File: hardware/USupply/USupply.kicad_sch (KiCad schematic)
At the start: 11 parts, among them P1 USB_C_Receptacle_USB2.0, Q1 Si2319CDS, U1 HUSB238

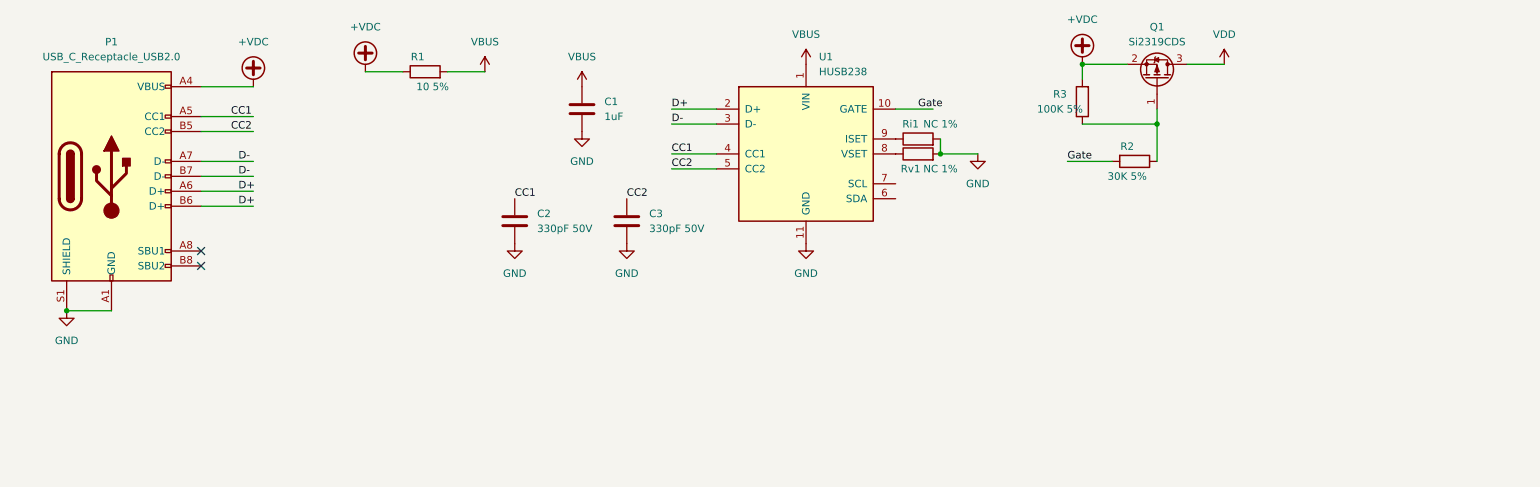
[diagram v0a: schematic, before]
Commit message: refactor(hw/usb): refine usb pd by sub
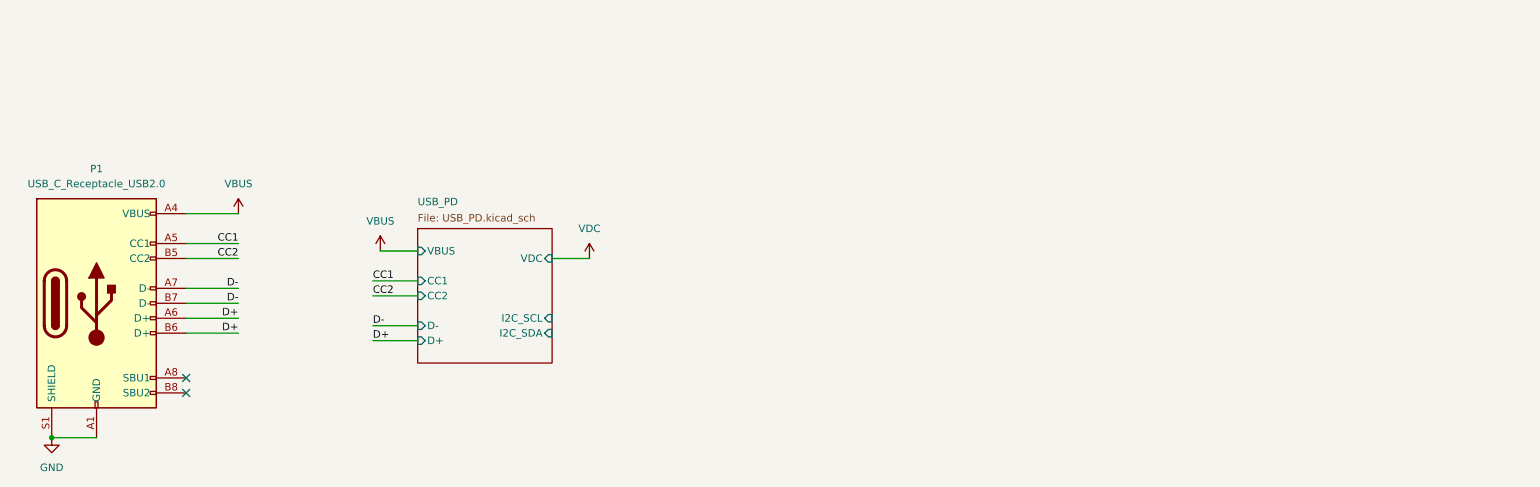
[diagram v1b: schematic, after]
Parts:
- removed C1: 1uF, Capacitor_SMD:C_0603_1608Metric_Pad1.08x0.95mm_HandSolder, symbol Device:C
- removed C2, C3: 330pF 50V, Capacitor_SMD:C_0603_1608Metric_Pad1.08x0.95mm_HandSolder, symbol Device:C
- removed Q1: Si2319CDS, Package_TO_SOT_SMD:SOT-23, symbol Transistor_FET:Si2319CDS
- removed R1: 10 5%, Resistor_SMD:R_0603_1608Metric, symbol Device:R
- removed R2: 30K 5%, Resistor_SMD:R_0603_1608Metric, symbol Device:R
- removed R3: 100K 5%, Resistor_SMD:R_0603_1608Metric, symbol Device:R
- removed Ri1, Rv1: NC 1%, Resistor_SMD:R_0603_1608Metric, symbol Device:R
- removed U1: HUSB238, Package_DFN_QFN:DFN-10-1EP_3x3mm_P0.5mm_EP1.7x2.5mm, symbol Power_Management:STM6600
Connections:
- net +VDC is gone; now on net VBUS: P1.A4 (VBUS), P1.A9 (VBUS), P1.B4 (VBUS), P1.B9 (VBUS)
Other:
- added sheet USB_PD (USB_PD.kicad_sch)

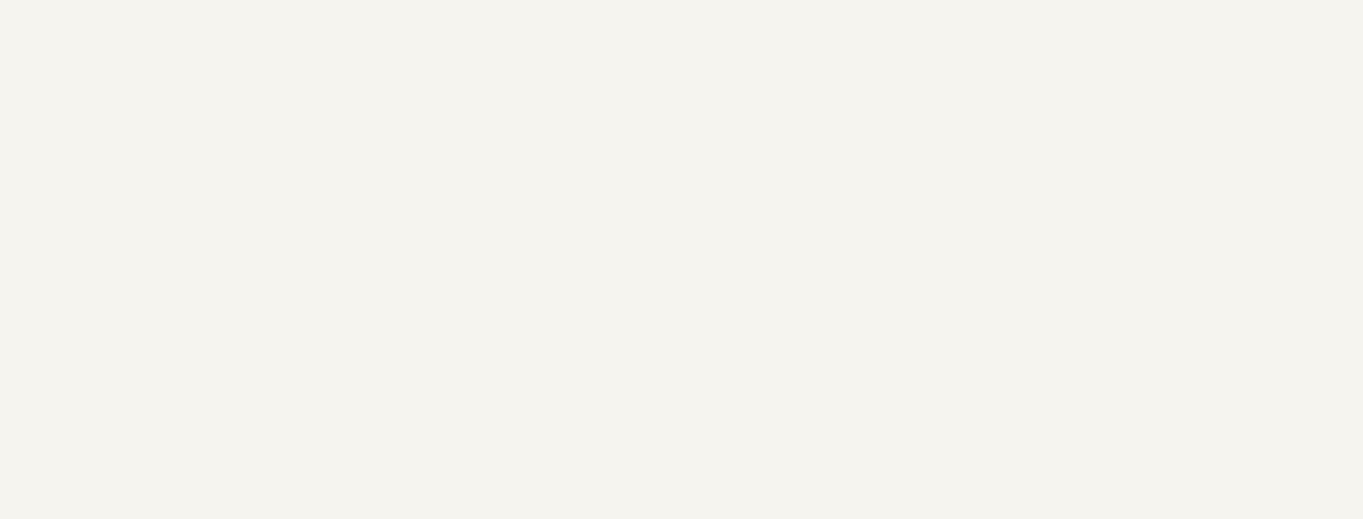
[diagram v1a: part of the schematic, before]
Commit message: feat(hw/usb): update usb pd circuit
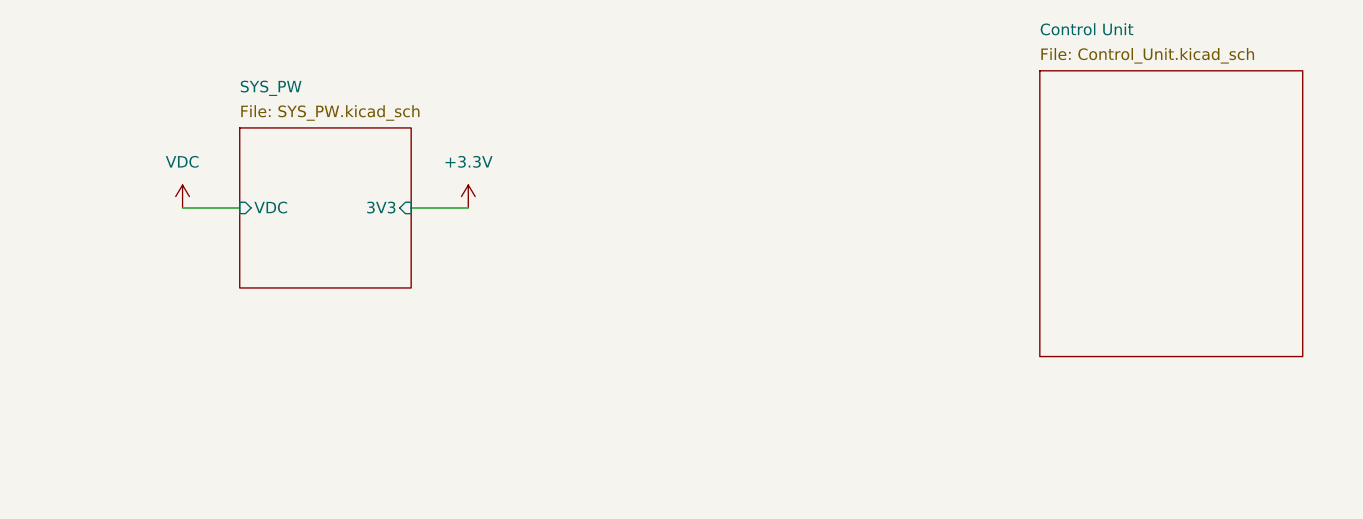
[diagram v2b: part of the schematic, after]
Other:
- added sheet Control Unit (Control_Unit.kicad_sch)
- added sheet SYS_PW (SYS_PW.kicad_sch)
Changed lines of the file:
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@@
+    (stroke (width 0) (type default))
+  )
+  (wire (pts (xy 175.26 46.99) (xy 181.61 46.99))
     (stroke (width 0) (type default))
   )
@@
     (stroke (width 0) (type default))
   )
+  (wire (pts (xy 156.21 46.99) (xy 149.86 46.99))
+    (stroke (width 0) (type default))
+  )
   (wire (pts (xy 113.03 60.96) (xy 119.38 60.96))
     (stroke (width 0) (type default))
@@
     (effects (font (size 1.27 1.27)) (justify left bottom))
   )
+  (symbol (lib_id "power:+3.3V") (at 181.61 46.99 0) (unit 1)
+    (in_bom yes) (on_board yes) (dnp no) (fields_autoplaced)
+    (property "Reference" "#PWR03" (at 181.61 50.8 0)
+      (effects (font (size 1.27 1.27)) hide)
+    )
+    (property "Value" "+3.3V" (at 181.61 41.91 0)
+      (effects (font (size 1.27 1.27)))
+    )
+    (property "Footprint" "" (at 181.61 46.99 0)
+      (effects (font (size 1.27 1.27)) hide)
+    )
+    (property "Datasheet" "" (at 181.61 46.99 0)
+      (effects (font (size 1.27 1.27)) hide)
+    )
+    (pin "1")
+    (instances
+      (project "USupply"
+        (path "/3b676929-25bc-45bd-b040-e1f1ea265704"
+          (reference "#PWR03") (unit 1)
+        )
+      )
+    )
+  )
   (symbol (lib_id "power:VDC") (at 119.38 60.96 0) (unit 1)
     (in_bom yes) (on_board yes) (dnp no) (fields_autoplaced)
@@
         (path "/3b676929-25bc-45bd-b040-e1f1ea265704"
           (reference "#PWR06") (unit 1)
+        )
+      )
+    )
+  )
+  (symbol (lib_id "power:VDC") (at 149.86 46.99 0) (mirror y) (unit 1)
+    (in_bom yes) (on_board yes) (dnp no) (fields_autoplaced)
+    (property "Reference" "#PWR02" (at 149.86 49.53 0)
+      (effects (font (size 1.27 1.27)) hide)
+    )
+    (property "Value" "VDC" (at 149.86 41.91 0)
+      (effects (font (size 1.27 1.27)))
+    )
+    (property "Footprint" "" (at 149.86 46.99 0)
+      (effects (font (size 1.27 1.27)) hide)
+    )
+    (property "Datasheet" "" (at 149.86 46.99 0)
+      (effects (font (size 1.27 1.27)) hide)
+    )
+    (pin "1")
+    (instances
+      (project "USupply"
+        (path "/3b676929-25bc-45bd-b040-e1f1ea265704"
+          (reference "#PWR02") (unit 1)
         )
       )
@@
       )
     )
+  )
+  (sheet (at 156.21 38.1) (size 19.05 17.78)
+    (stroke (width 0.1524) (type solid))
+    (fill (color 0 0 0 0.0000))
+    (property "Sheetname" "SYS_PW" (at 156.21 34.29 0)
+      (effects (font (size 1.27 1.27)) (justify left bottom))
+    )
+    (property "Sheetfile" "SYS_PW.kicad_sch" (at 156.21 35.56 0)
+      (effects (font (size 1.27 1.27)) (justify left top))
+    )
+    (pin "VDC" input (at 156.21 46.99 180)
+      (effects (font (size 1.27 1.27)) (justify left))
+    )
+    (pin "3V3" input (at 175.26 46.99 0)
+      (effects (font (size 1.27 1.27)) (justify right))
+    )
+    (instances
+      (project "USupply"
+        (path "/3b676929-25bc-45bd-b040-e1f1ea265704" (page "3"))
+      )
+    )
+  )
+  (sheet (at 245.11 31.75) (size 29.21 31.75)
+    (stroke (width 0.1524) (type solid))
+    (fill (color 0 0 0 0.0000))
+    (property "Sheetname" "Control Unit" (at 245.11 27.94 0)
+      (effects (font (size 1.27 1.27)) (justify left bottom))
+    )
+    (property "Sheetfile" "Control_Unit.kicad_sch" (at 245.11 29.21 0)
+      (effects (font (size 1.27 1.27)) (justify left top))
+    )
+    (instances
+      (project "USupply"
+        (path "/3b676929-25bc-45bd-b040-e1f1ea265704" (page "4"))
+      )
+    )

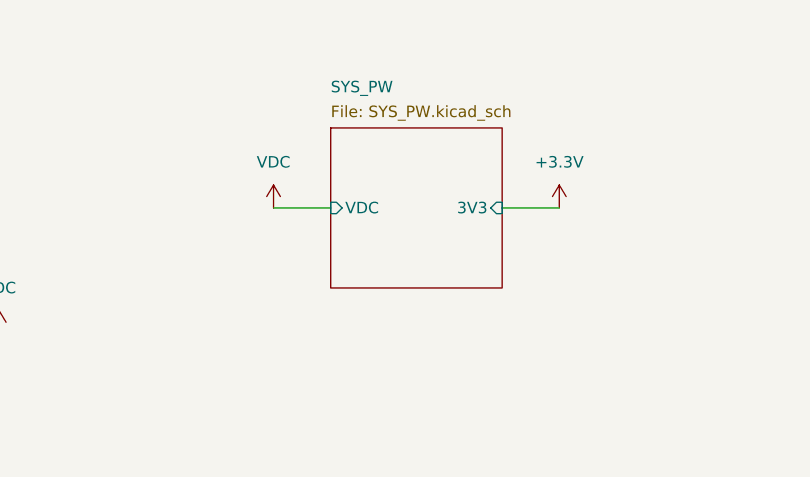
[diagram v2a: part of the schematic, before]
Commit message: feat(hw/usb): update 3.3v circuit
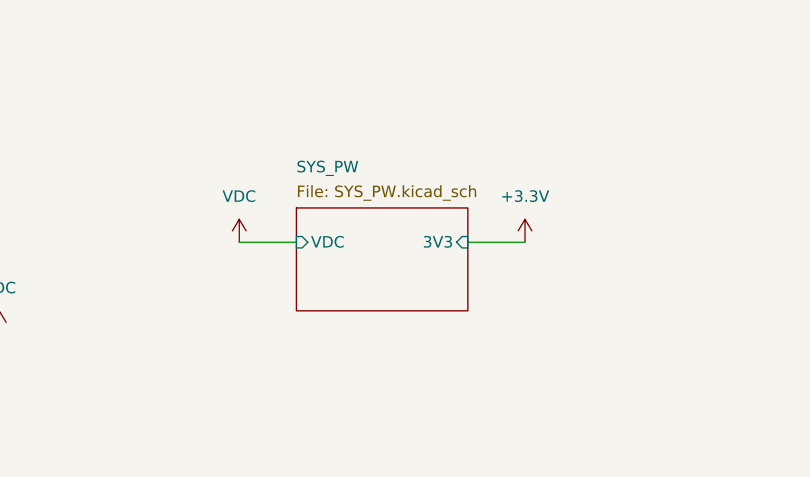
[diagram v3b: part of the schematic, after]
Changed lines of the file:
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@@
     (stroke (width 0) (type default))
   )
-  (wire (pts (xy 175.26 46.99) (xy 181.61 46.99))
+  (wire (pts (xy 171.45 50.8) (xy 177.8 50.8))
     (stroke (width 0) (type default))
   )
@@
     (stroke (width 0) (type default))
   )
-  (wire (pts (xy 156.21 46.99) (xy 149.86 46.99))
-    (stroke (width 0) (type default))
-  )
   (wire (pts (xy 113.03 60.96) (xy 119.38 60.96))
     (stroke (width 0) (type default))
@@
     (stroke (width 0) (type default))
   )
+  (wire (pts (xy 146.05 50.8) (xy 152.4 50.8))
+    (stroke (width 0) (type default))
+  )
   (label "D+" (at 82.55 74.93 0) (fields_autoplaced)
     (effects (font (size 1.27 1.27)) (justify left bottom))
@@
     (effects (font (size 1.27 1.27)) (justify left bottom))
   )
-  (symbol (lib_id "power:+3.3V") (at 181.61 46.99 0) (unit 1)
-    (in_bom yes) (on_board yes) (dnp no) (fields_autoplaced)
-    (property "Reference" "#PWR03" (at 181.61 50.8 0)
-      (effects (font (size 1.27 1.27)) hide)
-    )
-    (property "Value" "+3.3V" (at 181.61 41.91 0)
-      (effects (font (size 1.27 1.27)))
-    )
-    (property "Footprint" "" (at 181.61 46.99 0)
-      (effects (font (size 1.27 1.27)) hide)
-    )
-    (property "Datasheet" "" (at 181.61 46.99 0)
+  (symbol (lib_id "power:+3.3V") (at 177.8 50.8 0) (unit 1)
+    (in_bom yes) (on_board yes) (dnp no) (fields_autoplaced)
+    (property "Reference" "#PWR03" (at 177.8 54.61 0)
+      (effects (font (size 1.27 1.27)) hide)
+    )
+    (property "Value" "+3.3V" (at 177.8 45.72 0)
+      (effects (font (size 1.27 1.27)))
+    )
+    (property "Footprint" "" (at 177.8 50.8 0)
+      (effects (font (size 1.27 1.27)) hide)
+    )
+    (property "Datasheet" "" (at 177.8 50.8 0)
       (effects (font (size 1.27 1.27)) hide)
     )
@@
     )
   )
-  (symbol (lib_id "power:VDC") (at 149.86 46.99 0) (mirror y) (unit 1)
-    (in_bom yes) (on_board yes) (dnp no) (fields_autoplaced)
-    (property "Reference" "#PWR02" (at 149.86 49.53 0)
-      (effects (font (size 1.27 1.27)) hide)
-    )
-    (property "Value" "VDC" (at 149.86 41.91 0)
-      (effects (font (size 1.27 1.27)))
-    )
-    (property "Footprint" "" (at 149.86 46.99 0)
-      (effects (font (size 1.27 1.27)) hide)
-    )
-    (property "Datasheet" "" (at 149.86 46.99 0)
+  (symbol (lib_id "power:VDC") (at 146.05 50.8 0) (mirror y) (unit 1)
+    (in_bom yes) (on_board yes) (dnp no) (fields_autoplaced)
+    (property "Reference" "#PWR02" (at 146.05 53.34 0)
+      (effects (font (size 1.27 1.27)) hide)
+    )
+    (property "Value" "VDC" (at 146.05 45.72 0)
+      (effects (font (size 1.27 1.27)))
+    )
+    (property "Footprint" "" (at 146.05 50.8 0)
+      (effects (font (size 1.27 1.27)) hide)
+    )
+    (property "Datasheet" "" (at 146.05 50.8 0)
       (effects (font (size 1.27 1.27)) hide)
     )
@@
     )
   )
-  (sheet (at 156.21 38.1) (size 19.05 17.78)
+  (sheet (at 152.4 46.99) (size 19.05 11.43)
     (stroke (width 0.1524) (type solid))
     (fill (color 0 0 0 0.0000))
-    (property "Sheetname" "SYS_PW" (at 156.21 34.29 0)
+    (property "Sheetname" "SYS_PW" (at 152.4 43.18 0)
       (effects (font (size 1.27 1.27)) (justify left bottom))
     )
-    (property "Sheetfile" "SYS_PW.kicad_sch" (at 156.21 35.56 0)
+    (property "Sheetfile" "SYS_PW.kicad_sch" (at 152.4 44.45 0)
       (effects (font (size 1.27 1.27)) (justify left top))
     )
-    (pin "VDC" input (at 156.21 46.99 180)
+    (pin "VDC" input (at 152.4 50.8 180)
       (effects (font (size 1.27 1.27)) (justify left))
     )
-    (pin "3V3" input (at 175.26 46.99 0)
+    (pin "3V3" input (at 171.45 50.8 0)
       (effects (font (size 1.27 1.27)) (justify right))
     )
